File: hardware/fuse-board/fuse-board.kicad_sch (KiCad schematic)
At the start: 43 parts, among them J1 BUS+ IN, J10 W8, J11 SPARE, J12 W21, J13 W22, J14 24V IN, J15 STAR, J16 FRAME, J17 I2C GH, J2 W10, J3 W11, J4 W12, J5 W13, J6 W14, J7 W15, J8 W16, J9 W17, U1 INA228

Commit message: Body B5: the board's numbers, its facts for the body, and its catalogue entries
hardware/fuse-board/analysis.py: every branch's copper against its fuse (IPC-2221 per layer: the 6 mm runs on both
layers rise 4 C at 20 A and 11 C at 30 A; the 2.6 mm necks past the holders' pegs add under 0.5 C), the main path
(continuous 40 A, the 80 A jump pulse adds 2-3 C), the copper against each fuse's let-through, the INA228's error
budget (within 1 % from 2 A to 80 A after the bring-up's one-point calibration; 2.0-2.5 % worst case without it),
the mass (132 g with hardware and standoffs). measure.py reads the filled board's copper for it.
cad/body_fuse_board.py: the envelope in the robot frame (x 34..122, y -14..62, z 138.2..174.2), the holders, the
studs and pads with their wires, the mounting (MH1 into the plate's nut at (50, 47), three ties), the P3 wire rows
(W4, W5, W8, W9, W10-W17, W21-W23, W27, W33 changed; W40-W42 new; W6, W30-W32 gone) and the order ($156.70 for one
board built, the 5-board PCB order and the pack hardware included).
catalog/body.json: 18 entries appended (the PCB, the Littelfuse MINI FL1 holder, the Bourns 1 mOhm shunt, the bare
INA228, the GH header and housing, three Ancor #8 rings, five McMaster parts, four LCSC passives), each with two
sellers read on 2026-10-27. The generator now writes the board with content-derived UUIDs: rebuilds are identical.

Co-Authored-By: Claude Opus 5.5 <noreply@anthropic.com>
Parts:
- J14: Wires W_24: DDR-120C-24 +V (18 AWG) -> W40 DDR-120C-24 +V (18 AWG)
- J15: Wires W23 DDR-120C-24 -V; W27 DDR-60L-12 -V; W_STAR: - bus bar ta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 -> W23 DDR-120C-24 -V; W27 DDR-60L-12 -V; W41 - bus bar tap 5 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
- J16: Wires W33 frame bond (18 AWG green) -> W33 frame bond (14 AWG green)
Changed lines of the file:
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@@
 			)
 		)
-		(property "Wires" "W_24: DDR-120C-24 +V (18 AWG)"
+		(property "Wires" "W40 DDR-120C-24 +V (18 AWG)"
 			(at 30.48 162.56 0)
 			(effects
@@
 			)
 		)
-		(property "Wires" "W23 DDR-120C-24 -V; W27 DDR-60L-12 -V; W_STAR: - bus bar tap 5 (14 AWG)"
+		(property "Wires" "W23 DDR-120C-24 -V; W27 DDR-60L-12 -V; W41 - bus bar tap 5 (14 AWG)"
 			(at 330.2 165.1 0)
 			(effects
@@
 			)
 		)
-		(property "Wires" "W33 frame bond (18 AWG green)"
+		(property "Wires" "W33 frame bond (14 AWG green)"
 			(at 330.2 180.34 0)
 			(effects

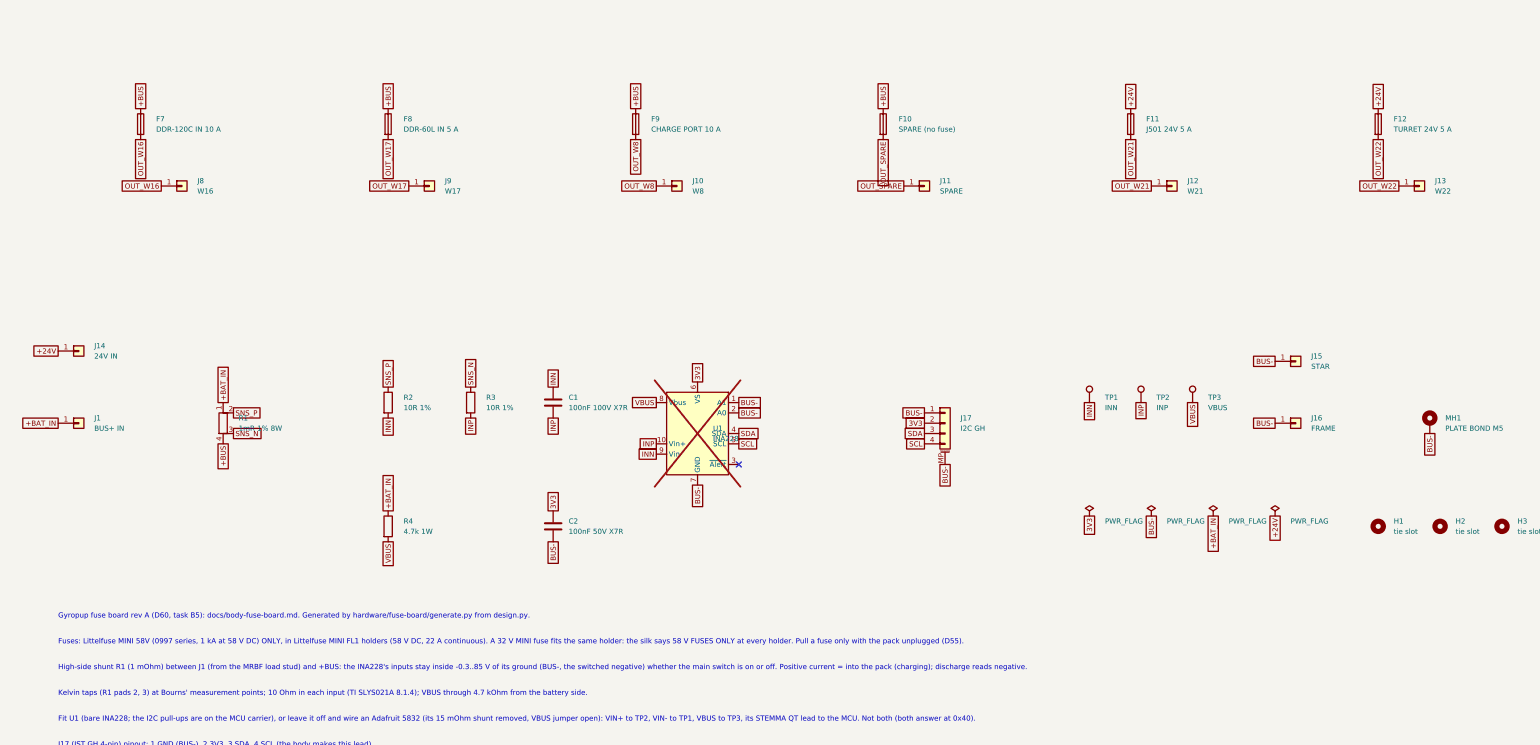
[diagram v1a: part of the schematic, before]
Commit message: Body B5 for D65 and D66: the fuse board on the 10S bus with the TRACO 12 V rail and the turret's own feed
Holders: F7 the TRACO TEP 150-4812WI's input (W16, 10 A); F8 the turret's feed from the + bus through the stop
relay's pole B (W22, 7.5 A: keeps the G2RL-2's contact under its 8 A carry; its 2-pole DC curve holds about 6 A at
41 V, the turret's 140 W burst is 3.4 A there); F9, F10 spares (no charge port under D65); the 24 V island becomes the
12 V rail (J14 12V IN from the TRACO, W40 14 AWG, 12.5 A at +0.4 C in the pour): F11 the J501 at 12 V (W21, 10 A), F12
the rest of the rail (W43, 7.5 A). Same outline, mounting and copper; DRC, ERC and parity clean; JLCPCB's price
re-read on the new zip: $40.60 for 5. cad/body_fuse_board.py's P3 rows and order follow ($154.48 for one board),
the 7.5 A MINI 58V fuse appended to the catalogue, the doc revised with the relay's rating, the arrival checks and
the plate's third tie slot (40c427b moved it from y 24 to 18, under F12).

Co-Authored-By: Claude Opus 5.5 <noreply@anthropic.com>
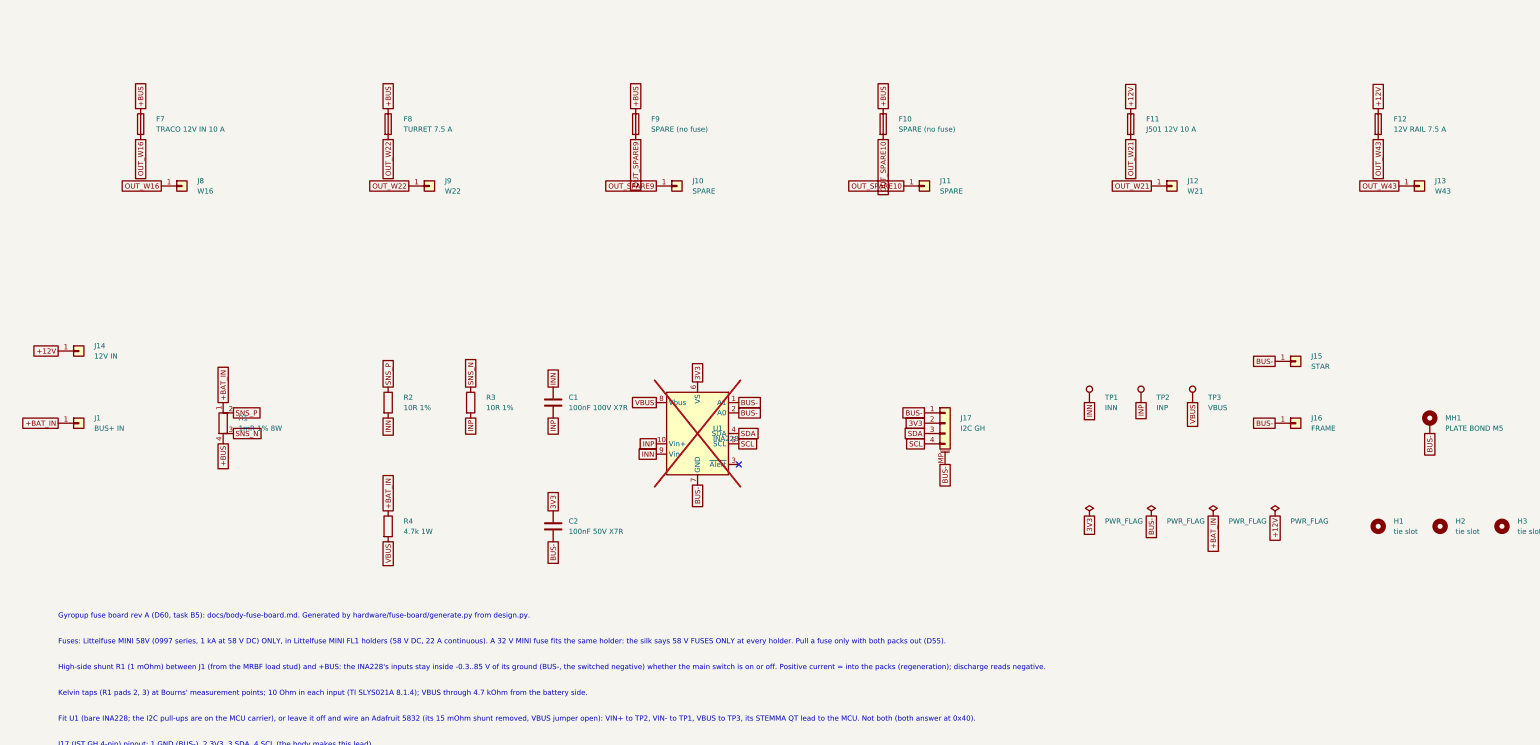
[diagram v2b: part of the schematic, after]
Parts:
- F11: value J501 24V 5 A -> J501 12V 10 A; Fuse Littelfuse 0997005.WXN MINI 58V 5 A -> Littelfuse 0997010.WXN MINI 58V 10 A
- F12: value TURRET 24V 5 A -> 12V RAIL 7.5 A; Fuse Littelfuse 0997005.WXN MINI 58V 5 A -> Littelfuse 099707.5.WXN MINI 58V 7.5 A; Wire W22 -> W43
- F7: value DDR-120C IN 10 A -> TRACO 12V IN 10 A
- F8: value DDR-60L IN 5 A -> TURRET 7.5 A; Fuse Littelfuse 0997005.WXN MINI 58V 5 A -> Littelfuse 099707.5.WXN MINI 58V 7.5 A; Wire W17 -> W22
- F9: value CHARGE PORT 10 A -> SPARE (no fuse); Fuse Littelfuse 0997010.WXN MINI 58V 10 A -> none (spare); Wire W8 -> -
- J10: value W8 -> SPARE; Wires W8 charge port + -> (spare)
- J12: Wires W21 J501 DC-IN -> W21 J501 DC-IN (12 V)
- J13: value W22 -> W43; Wires W22 stop relay pole B -> W43 the 12 V rail (lidar box, SSC1, eyes, 5 V buck)
- J14: value 24V IN -> 12V IN; Wires W40 DDR-120C-24 +V (18 AWG) -> W40 TRACO TEP 150-4812WI +V (14 AWG)
- J15: Wires W23 DDR-120C-24 -V; W27 DDR-60L-12 -V; W41 - bus bar tap 5 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 -> W23 TRACO -V (the 12 V return's tie); W41 - bus bar tap 5 (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
- J8: Wires W16 DDR-120C-24 Vin+ -> W16 TRACO TEP 150-4812WI Vin+
- J9: value W17 -> W22; Wires W17 DDR-60L-12 Vin+ -> W22 stop relay pole B (in), then the turret's XT30
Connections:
- net OUT_W17 is gone; now on net OUT_W22: F8.2, J9.1 (Pin_1)
- net OUT_W22: no longer F12.2, J13.1 (Pin_1)
- net +24V renamed +12V
- net OUT_SPARE renamed OUT_SPARE10
- net OUT_W8 renamed OUT_SPARE9
- new net OUT_W43: F12.2, J13.1 (Pin_1)
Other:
- note added: "Fuses: Littelfuse MINI 58V (0997 series, 1 kA at 58 V DC) ONLY, in Littelfuse MINI FL1 holders (58 V DC, 22 A continuous). A 32 V MINI fuse fits the same holder: the silk says 58 V FUSES ONLY at every holder. Pull a fuse only with both packs out (D55)."
- note added: "High-side shunt R1 (1 mOhm) between J1 (from the MRBF load stud) and +BUS: the INA228's inputs stay inside -0.3..85 V of its ground (BUS-, the switched negative) whether the main switch is on or off. Positive current = into the packs (regeneration); discharge reads negative."
- note removed: "Fuses: Littelfuse MINI 58V (0997 series, 1 kA at 58 V DC) ONLY, in Littelfuse MINI FL1 holders (58 V DC, 22 A continuous). A 32 V MINI fuse fits the same holder: the silk says 58 V FUSES ONLY at every holder. Pull a fuse only with the pack unplugged (D55)."
- note removed: "High-side shunt R1 (1 mOhm) between J1 (from the MRBF load stud) and +BUS: the INA228's inputs stay inside -0.3..85 V of its ground (BUS-, the switched negative) whether the main switch is on or off. Positive current = into the pack (charging); discharge reads negative."
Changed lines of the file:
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@@
 			)
 		)
-		(property "Value" "J501 24V 5 A"
+		(property "Value" "J501 12V 10 A"
 			(at 293.37 107.95 0)
 			(effects
@@
 			)
 		)
-		(property "Fuse" "Littelfuse 0997005.WXN MINI 58V 5 A"
+		(property "Fuse" "Littelfuse 0997010.WXN MINI 58V 10 A"
 			(at 289.56 106.68 0)
 			(effects
@@
 			)
 		)
-		(property "Value" "TURRET 24V 5 A"
+		(property "Value" "12V RAIL 7.5 A"
 			(at 354.33 107.95 0)
 			(effects
@@
 			)
 		)
-		(property "Fuse" "Littelfuse 0997005.WXN MINI 58V 5 A"
+		(property "Fuse" "Littelfuse 099707.5.WXN MINI 58V 7.5 A"
 			(at 350.52 106.68 0)
 			(effects
@@
 			)
 		)
-		(property "Wire" "W22"
+		(property "Wire" "W43"
 			(at 350.52 106.68 0)
 			(effects
@@
 			)
 		)
-		(property "Value" "DDR-120C IN 10 A"
+		(property "Value" "TRACO 12V IN 10 A"
 			(at 49.53 107.95 0)
 			(effects
@@
 			)
 		)
-		(property "Value" "DDR-60L IN 5 A"
+		(property "Value" "TURRET 7.5 A"
 			(at 110.49 107.95 0)
 			(effects
@@
 			)
 		)
-		(property "Fuse" "Littelfuse 0997005.WXN MINI 58V 5 A"
+		(property "Fuse" "Littelfuse 099707.5.WXN MINI 58V 7.5 A"
 			(at 106.68 106.68 0)
 			(effects
@@
 			)
 		)
-		(property "Wire" "W17"
+		(property "Wire" "W22"
 			(at 106.68 106.68 0)
 			(effects
@@
 			)
 		)
-		(property "Value" "CHARGE PORT 10 A"
+		(property "Value" "SPARE (no fuse)"
 			(at 171.45 107.95 0)
 			(effects
@@
 			)
 		)
-		(property "Fuse" "Littelfuse 0997010.WXN MINI 58V 10 A"
+		(property "Fuse" "none (spare)"
 			(at 167.64 106.68 0)
 			(effects
@@
 			)
 		)
-		(property "Wire" "W8"
+		(property "Wire" "-"
 			(at 167.64 106.68 0)
 			(effects
@@
 			)
 		)
-		(property "Value" "W8"
+		(property "Value" "SPARE"
 			(at 181.61 123.19 0)
 			(effects
@@
 			)
 		)
-		(property "Wires" "W8 charge port +"
+		(property "Wires" "(spare)"
 			(at 177.8 121.92 0)
 			(effects
@@
 			)
 		)
-		(property "Wires" "W21 J501 DC-IN"
+		(property "Wires" "W21 J501 DC-IN (12 V)"
 			(at 299.72 121.92 0)
 			(effects
@@
 			)
 		)
-		(property "Value" "W22"
+		(property "Value" "W43"
 			(at 364.49 123.19 0)
 			(effects
@@
 			)
 		)
-		(property "Wires" "W22 stop relay pole B"
+		(property "Wires" "W43 the 12 V rail (lidar box, SSC1, eyes, 5 V buck)"
 			(at 360.68 121.92 0)
 			(effects
@@
 			)
 		)
-		(property "Value" "24V IN"
+		(property "Value" "12V IN"
 			(at 34.29 163.83 0)
 			(effects
@@
 			)
 		)
-		(property "Wires" "W40 DDR-120C-24 +V (18 AWG)"
+		(property "Wires" "W40 TRACO TEP 150-4812WI +V (14 AWG)"
 			(at 30.48 162.56 0)
 			(effects
@@
 			)
 		)
-		(property "Wires" "W23 DDR-120C-24 -V; W27 DDR-60L-12 -V; W41 - bus bar tap 5 (14 AWG)"
+		(property "Wires" "W23 TRACO -V (the 12 V return's tie); W41 - bus bar tap 5 (14 AWG)"
 			(at 330.2 165.1 0)
 			(effects
@@
 			)
 		)
-		(property "Wires" "W16 DDR-120C-24 Vin+"
+		(property "Wires" "W16 TRACO TEP 150-4812WI Vin+"
 			(at 55.88 121.92 0)
 			(effects
@@
 			)
 		)
-		(property "Value" "W17"
+		(property "Value" "W22"
 			(at 120.65 123.19 0)
 			(effects
@@
 			)
 		)
-		(property "Wires" "W17 DDR-60L-12 Vin+"
+		(property "Wires" "W22 stop relay pole B (in), then the turret's XT30"
 			(at 116.84 121.92 0)
 			(effects
@@
 		)
 	)
-	(global_label "+24V"
+	(global_label "+12V"
 		(shape passive)
 		(at 325.12 203.2 270)
@@
 		)
 	)
-	(global_label "OUT_SPARE"
+	(global_label "OUT_SPARE10"
 		(shape passive)
 		(at 228.6 110.49 270)
@@
 		)
 	)
-	(global_label "+24V"
+	(global_label "+12V"
 		(shape passive)
 		(at 289.56 102.87 90)
@@
 		)
 	)
-	(global_label "+24V"
+	(global_label "+12V"
 		(shape passive)
 		(at 350.52 102.87 90)
@@
 		)
 	)
-	(global_label "OUT_W22"
+	(global_label "OUT_W43"
 		(shape passive)
 		(at 350.52 110.49 270)
@@
 		)
 	)
-	(global_label "OUT_W17"
+	(global_label "OUT_W22"
 		(shape passive)
 		(at 106.68 110.49 270)
@@
 		)
 	)
-	(global_label "OUT_W8"
+	(global_label "OUT_SPARE9"
 		(shape passive)
 		(at 167.64 110.49 270)
@@
 		)
 	)
-	(global_label "OUT_W8"
+	(global_label "OUT_SPARE9"
 		(shape passive)
 		(at 172.72 121.92 180)
@@
 		)
 	)
-	(global_label "OUT_SPARE"
+	(global_label "OUT_SPARE10"
 		(shape passive)
 		(at 233.68 121.92 180)
@@
 		)
 	)
-	(global_label "OUT_W22"
+	(global_label "OUT_W43"
 		(shape passive)
 		(at 355.6 121.92 180)
@@
 		)
 	)
-	(global_label "+24V"
+	(global_label "+12V"
 		(shape passive)
 		(at 25.4 162.56 180)
@@
 		)
 	)
-	(global_label "OUT_W17"
+	(global_label "OUT_W22"
 		(shape passive)
 		(at 111.76 121.92 180)
@@
 		)
 	)
-	(text "Fuses: Littelfuse MINI 58V (0997 series, 1 kA at 58 V DC) ONLY, in Littelfuse MINI FL1 holders (58 V DC, 22 A continuous). A 32 V MINI fuse fits the same holder: the silk says 58 V FUSES ONLY at every holder. Pull a fuse only with the pack unplugged (D55)."
+	(text "Fuses: Littelfuse MINI 58V (0997 series, 1 kA at 58 V DC) ONLY, in Littelfuse MINI FL1 holders (58 V DC, 22 A continuous). A 32 V MINI fuse fits the same holder: the silk says 58 V FUSES ONLY at every holder. Pull a fuse only with both packs out (D55)."
 		(exclude_from_sim no)
 		(at 25.4 234.95 0)
@@
 		)
 	)
-	(text "High-side shunt R1 (1 mOhm) between J1 (from the MRBF load stud) and +BUS: the INA228's inputs stay inside -0.3..85 V of its ground (BUS-, the switched negative) whether the main switch is on or off. Positive current = into the pack (charging); discharge reads negative."
+	(text "High-side shunt R1 (1 mOhm) between J1 (from the MRBF load stud) and +BUS: the INA228's inputs stay inside -0.3..85 V of its ground (BUS-, the switched negative) whether the main switch is on or off. Positive current = into the packs (regeneration); discharge reads negative."
 		(exclude_from_sim no)
 		(at 25.4 241.3 0)
